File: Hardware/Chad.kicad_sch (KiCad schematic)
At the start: 58 parts, among them J1 RBUS, J2 GPIO Breakout, J3 ServoCH1, J4 ServoCH2, U1 ESP32-S3, Y1 R940000171

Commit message: Maybe chad v3.0 hardware
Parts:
- added D3: ~, Package_TO_SOT_SMD:SOT-353_SC-70-5, symbol iclr:CPDV5-3V3UP
- added R40, R41: TBD, Resistor_SMD:R_0402_1005Metric, symbol Device:R_Small
- R28, R29, R30, R31, R32, R33: value DNP -> 10k; now not fitted
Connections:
- net GPIO4 is gone; now on net GPIO5: J2.7 (Pin_7), R32.2, U1.10 (GPIO5/ADC1_CH4)
- net GND: now also D3.4, D3.5
- net GPIO5: no longer J2.8 (Pin_8), R33.2, U1.11 (GPIO6/ADC1_CH5)
- net Servo1PWM: now also D3.3, R40.1; no longer J3.3 (Pin_3)
- net Servo2PWM: now also D3.1, R41.1; no longer J4.3 (Pin_3)
- net +12V renamed 16.8V
- net GPIO0 renamed GPIO10
- net GPIO1 renamed GPIO8
- net GPIO2 renamed GPIO9
- net GPIO3 renamed GPIO7
- new net: J3.3 (Pin_3), R40.2
- new net: J4.3 (Pin_3), R41.2
- new net: D3.2, D3.2
- new net GPIO6: J2.8 (Pin_8), R33.2, U1.11 (GPIO6/ADC1_CH5)

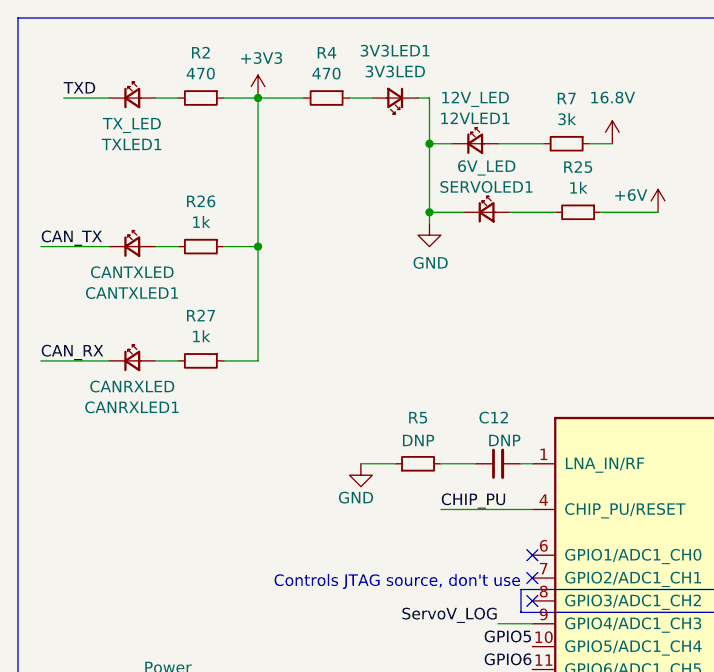
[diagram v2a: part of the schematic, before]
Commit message: 30V compatibility update
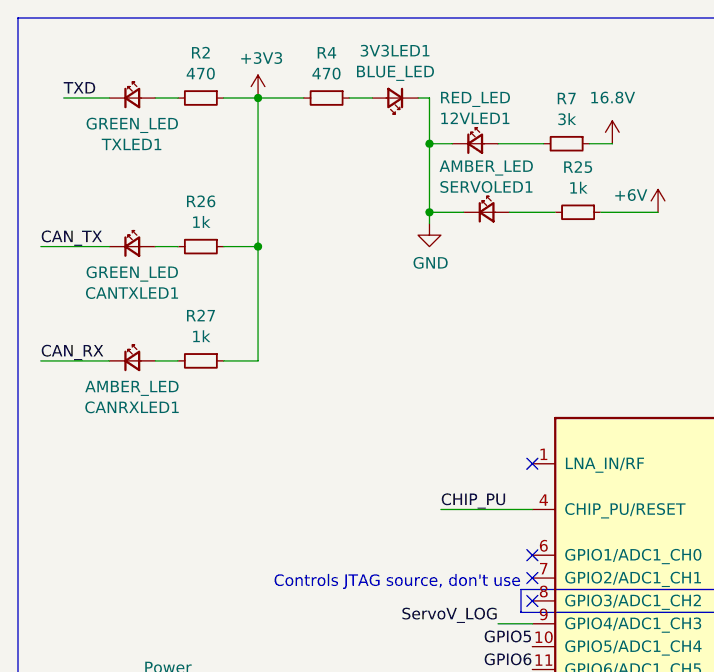
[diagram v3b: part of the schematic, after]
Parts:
- removed C12: DNP, Capacitor_SMD:C_0402_1005Metric, symbol Device:C_Small
- removed R5: DNP, Resistor_SMD:R_0402_1005Metric, symbol Device:R_Small
- 12VLED1: value 12V_LED -> RED_LED
- 3V3LED1: value 3V3LED -> BLUE_LED
- CANRXLED1: value CANRXLED -> AMBER_LED
- CANTXLED1: value CANTXLED -> GREEN_LED
- J1: footprint Connector_Molex:Molex_Mini-Fit_Jr_5569-06A2_2x03_P4.20mm_Horizontal -> iclr:Molex_Mini-Fit_Jr_5569-06A2_2x03_P4.20mm_Horizontal
- J3, J4: footprint Connector_Molex:Molex_Nano-Fit_105313-xx03_1x03_P2.50mm_Horizontal -> iclr:Molex_Nano-Fit_105313-xx03_1x03_P2.50mm_Horizontal
- R6: MPN (none) -> AC0402FR-07499RL
- SERVOLED1: value 6V_LED -> AMBER_LED
- TXLED1: value TX_LED -> GREEN_LED
- Y1: footprint Crystal:Crystal_SMD_2016-4Pin_2.0x1.6mm -> iclr:Crystal_SMD_2016-4Pin_2.0x1.6mm
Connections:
- no-connect marks 29 -> 30
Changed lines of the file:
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@@
 	)
 	(no_connect
+		(at 69.85 62.23)
+	)
+	(no_connect
 		(at 69.85 74.93)
 	)
@@
 	(wire
 		(pts
-			(xy 68.58 62.23) (xy 69.85 62.23)
-		)
-		(stroke
-			(width 0)
-			(type default)
-		)
-	)
-	(wire
-		(pts
 			(xy 27.94 21.59) (xy 30.48 21.59)
 		)
@@
 	(wire
 		(pts
-			(xy 50.8 62.23) (xy 54.61 62.23)
-		)
-		(stroke
-			(width 0)
-			(type default)
-		)
-	)
-	(wire
-		(pts
-			(xy 59.69 62.23) (xy 63.5 62.23)
-		)
-		(stroke
-			(width 0)
-			(type default)
-		)
-	)
-	(wire
-		(pts
 			(xy 207.01 46.99) (xy 207.01 49.53)
 		)
@@
 			)
 		)
-		(property "Value" "TX_LED"
+		(property "Value" "GREEN_LED"
 			(at 25.4 24.4856 0)
 			(effects
@@
 			)
 		)
-		(property "Value" "3V3LED"
+		(property "Value" "BLUE_LED"
 			(at 54.61 18.6944 0)
 			(effects
@@
 			)
 		)
-		(property "Footprint" "Connector_Molex:Molex_Mini-Fit_Jr_5569-06A2_2x03_P4.20mm_Horizontal"
+		(property "Footprint" "iclr:Molex_Mini-Fit_Jr_5569-06A2_2x03_P4.20mm_Horizontal"
 			(at 123.19 20.32 0)
 			(effects
@@
 			)
 		)
-		(property "Value" "12V_LED"
+		(property "Value" "RED_LED"
 			(at 63.5 21.59 0)
 			(effects
@@
 			)
 		)
-		(property "Footprint" "Connector_Molex:Molex_Nano-Fit_105313-xx03_1x03_P2.50mm_Horizontal"
+		(property "Footprint" "iclr:Molex_Nano-Fit_105313-xx03_1x03_P2.50mm_Horizontal"
 			(at 276.86 77.47 0)
 			(effects
@@
 			)
 		)
-		(property "Footprint" "Connector_Molex:Molex_Nano-Fit_105313-xx03_1x03_P2.50mm_Horizontal"
+		(property "Footprint" "iclr:Molex_Nano-Fit_105313-xx03_1x03_P2.50mm_Horizontal"
 			(at 276.86 92.71 0)
 			(effects
@@
 			)
 		)
-		(property "Value" "6V_LED"
+		(property "Value" "AMBER_LED"
 			(at 64.77 29.21 0)
 			(effects
@@
 	)
 	(symbol
-		(lib_id "Device:C_Small")
-		(at 66.04 62.23 90)
-		(unit 1)
-		(exclude_from_sim no)
-		(in_bom yes)
-		(on_board yes)
-		(dnp no)
-		(property "Reference" "C12"
-			(at 67.31 57.15 90)
-			(effects
-				(font
-					(size 1.27 1.27)
-				)
-				(justify left)
-			)
-		)
-		(property "Value" "DNP"
-			(at 68.58 59.69 90)
-			(effects
-				(font
-					(size 1.27 1.27)
-				)
-				(justify left)
-			)
-		)
-		(property "Footprint" "Capacitor_SMD:C_0402_1005Metric"
-			(at 66.04 62.23 0)
-			(effects
-				(font
-					(size 1.27 1.27)
-				)
-				(hide yes)
-			)
-		)
-		(property "Datasheet" "~"
-			(at 66.04 62.23 0)
-			(effects
-				(font
-					(size 1.27 1.27)
-				)
-				(hide yes)
-			)
-		)
-		(property "Description" ""
-			(at 66.04 62.23 0)
-			(effects
-				(font
-					(size 1.27 1.27)
-				)
-				(hide yes)
-			)
-		)
-		(pin "1"
-		)
-		(pin "2"
-		)
-		(instances
-			(project "Chad"
-				(path "/7db990e4-92e1-4f99-b4d2-435bbec1ba83"
-					(reference "C12")
-					(unit 1)
-				)
-			)
-		)
-	)
-	(symbol
 		(lib_id "Device:L")
 		(at 40.64 135.89 90)
@@
 			)
 		)
-		(property "Value" "CANTXLED"
+		(property "Value" "GREEN_LED"
 			(at 25.4 40.9956 0)
 			(effects
@@
 			)
 		)
-		(property "Footprint" "Crystal:Crystal_SMD_2016-4Pin_2.0x1.6mm"
+		(property "Footprint" "iclr:Crystal_SMD_2016-4Pin_2.0x1.6mm"
 			(at 156.21 132.08 0)
 			(effects
@@
 	)
 	(symbol
-		(lib_id "power:GND")
-		(at 50.8 62.23 0)
-		(unit 1)
-		(exclude_from_sim no)
-		(in_bom yes)
-		(on_board yes)
-		(dnp no)
-		(property "Reference" "#PWR09"
-			(at 50.8 68.58 0)
-			(effects
-				(font
-					(size 1.27 1.27)
-				)
-				(hide yes)
-			)
-		)
-		(property "Value" "GND"
-			(at 48.26 66.04 0)
-			(effects
-				(font
-					(size 1.27 1.27)
-				)
-				(justify left)
-			)
-		)
-		(property "Footprint" ""
-			(at 50.8 62.23 0)
-			(effects
-				(font
-					(size 1.27 1.27)
-				)
-				(hide yes)
-			)
-		)
-		(property "Datasheet" ""
-			(at 50.8 62.23 0)
-			(effects
-				(font
-					(size 1.27 1.27)
-				)
-				(hide yes)
-			)
-		)
-		(property "Description" ""
-			(at 50.8 62.23 0)
-			(effects
-				(font
-					(size 1.27 1.27)
-				)
-				(hide yes)
-			)
-		)
-		(pin "1"
-		)
-		(instances
-			(project "Chad"
-				(path "/7db990e4-92e1-4f99-b4d2-435bbec1ba83"
-					(reference "#PWR09")
-					(unit 1)
-				)
-			)
-		)
-	)
-	(symbol
 		(lib_id "Device:R_Small")
 		(at 59.69 113.03 90)
@@
 			)
 		)
+		(property "MPN" "AC0402FR-07499RL"
+			(at 59.69 113.03 90)
+			(effects
+				(font
+					(size 1.27 1.27)
+				)
+				(hide yes)
+			)
+		)
 		(pin "1"
 		)
@@
 			)
 		)
-		(property "Value" "CANRXLED"
+		(property "Value" "AMBER_LED"
 			(at 25.4 53.6956 0)
 			(effects
@@
 					(unit 1)
 				)
-			)
-		)
-	)
-	(symbol
-		(lib_id "Device:R_Small")
-		(at 57.15 62.23 90)
-		(unit 1)
-		(exclude_from_sim no)
-		(in_bom yes)
-		(on_board yes)
-		(dnp no)
-		(property "Reference" "R5"
-			(at 57.15 57.15 90)
-			(effects
-				(font
-					(size 1.27 1.27)
-				)
-			)
-		)
-		(property "Value" "DNP"
-			(at 57.15 59.69 90)
-			(effects
-				(font
-					(size 1.27 1.27)
-				)
-			)
-		)
-		(property "Footprint" "Resistor_SMD:R_0402_1005Metric"
-			(at 57.15 62.23 0)
-			(effects
-				(font
-					(size 1.27 1.27)
-				)
-				(hide yes)
-			)
-		)
-		(property "Datasheet" "~"
-			(at 57.15 62.23 0)
-			(effects
-				(font
-					(size 1.27 1.27)
-				)
-				(hide yes)
-			)
-		)
-		(property "Description" ""
-			(at 57.15 62.23 0)
-			(effects
-				(font
-					(size 1.27 1.27)
-				)
-				(hide yes)
-			)
-		)
-		(pin "1"
-		)
-		(pin "2"
-		)
-		(instances
-			(project "Chad"
-				(path "/7db990e4-92e1-4f99-b4d2-435bbec1ba83"
-					(reference "R5")
-					(unit 1)
-				)

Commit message: Resistor values
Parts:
- R40, R41: value TBD -> 165R; MPN (none) -> RK73H1ETTP1650F
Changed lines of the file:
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@@
 			)
 		)
-		(property "Value" "TBD"
+		(property "Value" "165R"
 			(at 266.7 72.39 90)
 			(effects
@@
 		(property "Description" "Resistor, small symbol"
 			(at 266.7 74.93 0)
+			(effects
+				(font
+					(size 1.27 1.27)
+				)
+				(hide yes)
+			)
+		)
+		(property "MPN" " RK73H1ETTP1650F "
+			(at 266.7 74.93 90)
 			(effects
 				(font
@@
 			)
 		)
-		(property "Value" "TBD"
+		(property "Value" "165R"
 			(at 266.7 87.63 90)
 			(effects
@@
 			(effects
 				(font
+					(size 1.27 1.27)
+				)
+				(hide yes)
+			)
+		)
+		(property "MPN" " RK73H1ETTP1650F "
+			(at 266.7 90.17 90)
+			(effects
+				(font

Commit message: Added GPIO TVS protection
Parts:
- removed D3: ~, Package_TO_SOT_SMD:SOT-353_SC-70-5, symbol iclr:CPDV5-3V3UP
- removed J2: GPIO Breakout, Connector_PinSocket_2.54mm:PinSocket_2x04_P2.54mm_Vertical, symbol Connector:Conn_01x08_Female
- removed J3: ServoCH1, iclr:Molex_Nano-Fit_105313-xx03_1x03_P2.50mm_Horizontal, symbol Connector:Conn_01x03_Male
- removed J4: ServoCH2, iclr:Molex_Nano-Fit_105313-xx03_1x03_P2.50mm_Horizontal, symbol Connector:Conn_01x03_Male
- removed R28, R29, R30, R31, R32, R33: 10k, Resistor_SMD:R_0402_1005Metric, symbol Device:R_Small
- removed R40, R41: 165R, Resistor_SMD:R_0402_1005Metric, symbol Device:R_Small
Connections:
- net Servo2PWM is gone; now on net Servo1PWM: U1.42 (GPIO37)
- net Servo1PWM: no longer U1.41 (GPIO36)
- new net Servo0PWM: U1.41 (GPIO36)
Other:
- added sheet GPIO (GPIO.kicad_sch)
- added sheet Servo Connectors (servo.kicad_sch)

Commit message: fixed pgood hardware issue
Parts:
- removed R35: 1.5k, Resistor_SMD:R_0402_1005Metric, symbol Device:R_Small
- R34: value 2.2k -> 18k
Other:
- sheet USB -> UART ports: added none; removed 3.3V
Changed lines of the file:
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@@
 	(wire
 		(pts
+			(xy 236.22 29.21) (xy 236.22 38.1)
+		)
+		(stroke
+			(width 0)
+			(type default)
+		)
+	)
+	(wire
+		(pts
 			(xy 156.21 127) (xy 156.21 128.27)
 		)
@@
 	(wire
 		(pts
-			(xy 236.22 34.29) (xy 236.22 38.1)
-		)
-		(stroke
-			(width 0)
-			(type default)
-		)
-	)
-	(wire
-		(pts
 			(xy 50.8 127) (xy 53.34 127)
 		)
@@
 	(wire
 		(pts
-			(xy 99.06 156.21) (xy 102.87 156.21)
-		)
-		(stroke
-			(width 0)
-			(type default)
-		)
-	)
-	(wire
-		(pts
 			(xy 167.64 138.43) (xy 166.37 138.43)
 		)
@@
 	)
 	(symbol
-		(lib_id "power:+3.3V")
-		(at 102.87 156.21 0)
-		(unit 1)
-		(exclude_from_sim no)
-		(in_bom yes)
-		(on_board yes)
-		(dnp no)
-		(property "Reference" "#PWR016"
-			(at 102.87 160.02 0)
-			(effects
-				(font
-					(size 1.27 1.27)
-				)
-				(hide yes)
-			)
-		)
-		(property "Value" "+3V3"
-			(at 103.251 151.8158 0)
-			(effects
-				(font
-					(size 1.27 1.27)
-				)
-			)
-		)
-		(property "Footprint" ""
-			(at 102.87 156.21 0)
-			(effects
-				(font
-					(size 1.27 1.27)
-				)
-				(hide yes)
-			)
-		)
-		(property "Datasheet" ""
-			(at 102.87 156.21 0)
-			(effects
-				(font
-					(size 1.27 1.27)
-				)
-				(hide yes)
-			)
-		)
-		(property "Description" ""
-			(at 102.87 156.21 0)
-			(effects
-				(font
-					(size 1.27 1.27)
-				)
-				(hide yes)
-			)
-		)
-		(pin "1"
-		)
-		(instances
-			(project "Chad"
-				(path "/7db990e4-92e1-4f99-b4d2-435bbec1ba83"
-					(reference "#PWR016")
-					(unit 1)
-				)
-			)
-		)
-	)
-	(symbol
 		(lib_id "power:GND")
 		(at 128.27 26.67 0)
@@
 	)
 	(symbol
-		(lib_id "Device:R_Small")
-		(at 236.22 31.75 180)
-		(unit 1)
-		(exclude_from_sim no)
-		(in_bom yes)
-		(on_board yes)
-		(dnp no)
-		(property "Reference" "R35"
-			(at 241.1984 31.75 90)
-			(effects
-				(font
-					(size 1.27 1.27)
-				)
-			)
-		)
-		(property "Value" "1.5k"
-			(at 238.887 31.75 90)
-			(effects
-				(font
-					(size 1.27 1.27)
-				)
-			)
-		)
-		(property "Footprint" "Resistor_SMD:R_0402_1005Metric"
-			(at 236.22 31.75 0)
-			(effects
-				(font
-					(size 1.27 1.27)
-				)
-				(hide yes)
-			)
-		)
-		(property "Datasheet" "~"
-			(at 236.22 31.75 0)
-			(effects
-				(font
-					(size 1.27 1.27)
-				)
-				(hide yes)
-			)
-		)
-		(property "Description" ""
-			(at 236.22 31.75 0)
-			(effects
-				(font
-					(size 1.27 1.27)
-				)
-				(hide yes)
-			)
-		)
-		(pin "1"
-		)
-		(pin "2"
-		)
-		(instances
-			(project "Chad"
-				(path "/7db990e4-92e1-4f99-b4d2-435bbec1ba83"
-					(reference "R35")
-					(unit 1)
-				)
-			)
-		)
-	)
-	(symbol
 		(lib_id "power:+6V")
 		(at 83.82 34.29 0)
@@
 			)
 		)
-		(property "Value" "2.2k"
+		(property "Value" "18k"
 			(at 238.887 40.64 90)
 			(effects
@@
 			)
 		)
-		(pin "3.3V" output
-			(at 99.06 156.21 0)
-			(effects
-				(font
-					(size 1.27 1.27)
-				)
-				(justify right)
-			)
-		)

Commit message: cleaned up schematic and bom
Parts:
- removed LOGO1: ICLR LOGO, iclr:iclr_logo_estd2018_10mm, symbol Mechanical:MountingHole_Pad
- C103: renamed from C3; value 0.1uF -> 100nF
- C105: renamed from C5; value 0.1uF -> 100nF
- C106: renamed from C6; value 0.1uF -> 100nF
- C108: renamed from C8; value 0.1uF -> 100nF
- C110: renamed from C10; value 0.1uF -> 100nF
- C111: renamed from C11; value 0.1uF -> 100nF
- C114: renamed from C45; value 0.1uF -> 100nF
- D101: renamed from TXLED1; value GREEN_LED -> LED_GREEN
- D102: renamed from CANTXLED1; value GREEN_LED -> LED_GREEN
- D103: renamed from CANRXLED1; value AMBER_LED -> LED_ORANGE
- D104: renamed from 3V3LED1; value BLUE_LED -> LED_BLUE
- D105: renamed from 12VLED1; value RED_LED -> LED_RED
- D106: renamed from SERVOLED1; value AMBER_LED -> LED_ORANGE
- H101: renamed from H1; now left out of the parts list
- H102: renamed from H2; now left out of the parts list
- H103: renamed from H3; now left out of the parts list
- H104: renamed from H4; now left out of the parts list
- L101: renamed from L1; value 2.0nH -> 2nH
- R101: renamed from R1; value 10K -> 10kΩ
- R102: renamed from R2; value 470 -> 470Ω
- R103: renamed from R26; value 1k -> 1kΩ
- R104: renamed from R27; value 1k -> 1kΩ
- R105: renamed from R3; value 10K -> 10kΩ
- R106: renamed from R4; value 470 -> 470Ω
- R107: renamed from R6; value 499 -> 499Ω
- R108: renamed from R7; value 3k -> 3kΩ
- R109: renamed from R25; value 1k -> 1kΩ
- R110: renamed from R36; value 1.5k -> 1.5kΩ
- R111: renamed from R37; value 470 -> 470Ω
- R112: renamed from R34; value 18k -> 18kΩ
- TP101: renamed from TP9; now left out of the parts list
- TP102: renamed from TP10; now left out of the parts list
- Y101: renamed from Y1; value R940000171 -> 40MHz; MPN (none) -> R940000171
- renumbered C1 to C101, C2 to C102, C4 to C104, C7 to C107, C9 to C109, C13 to C112, C14 to C113, ENJUMPER1 to J101, BOOTJUMPER1 to J102, J1 to J103, L2 to L102, U1 to U101
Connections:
- no-connect marks 30 -> 29

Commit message: continued
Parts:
- Y101: value 40MHz -> 40MHz±10ppm; footprint iclr:Crystal_SMD_2016-4Pin_2.0x1.6mm -> Crystal:Crystal_SMD_2016-4Pin_2.0x1.6mm
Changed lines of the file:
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@@
 			)
 		)
-		(property "Value" "40MHz"
+		(property "Value" "40MHz±10ppm"
 			(at 149.86 124.46 90)
 			(effects
@@
 			)
 		)
-		(property "Footprint" "iclr:Crystal_SMD_2016-4Pin_2.0x1.6mm"
+		(property "Footprint" "Crystal:Crystal_SMD_2016-4Pin_2.0x1.6mm"
 			(at 156.21 132.08 0)
 			(effects
